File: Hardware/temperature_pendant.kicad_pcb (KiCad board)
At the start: 2 copper layers, 25.4 x 20.3 mm, 5 parts, among them J1 CONN-6, SW1 SW-MOM, U1 BLINKM/MINM, U2 TMP3X

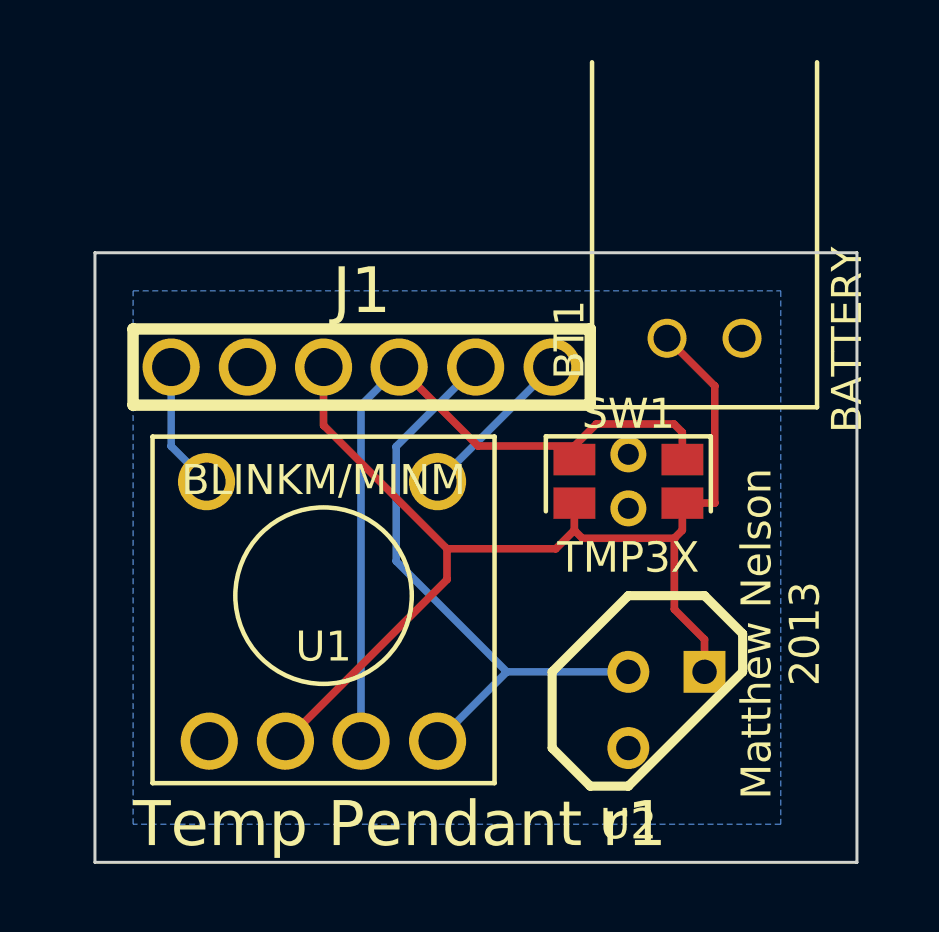
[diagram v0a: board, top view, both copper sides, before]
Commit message: Updated
Fixed same issues as in the bigger BlinkM version.  Re-did placement on
switch and battery connector.  Re-routed.
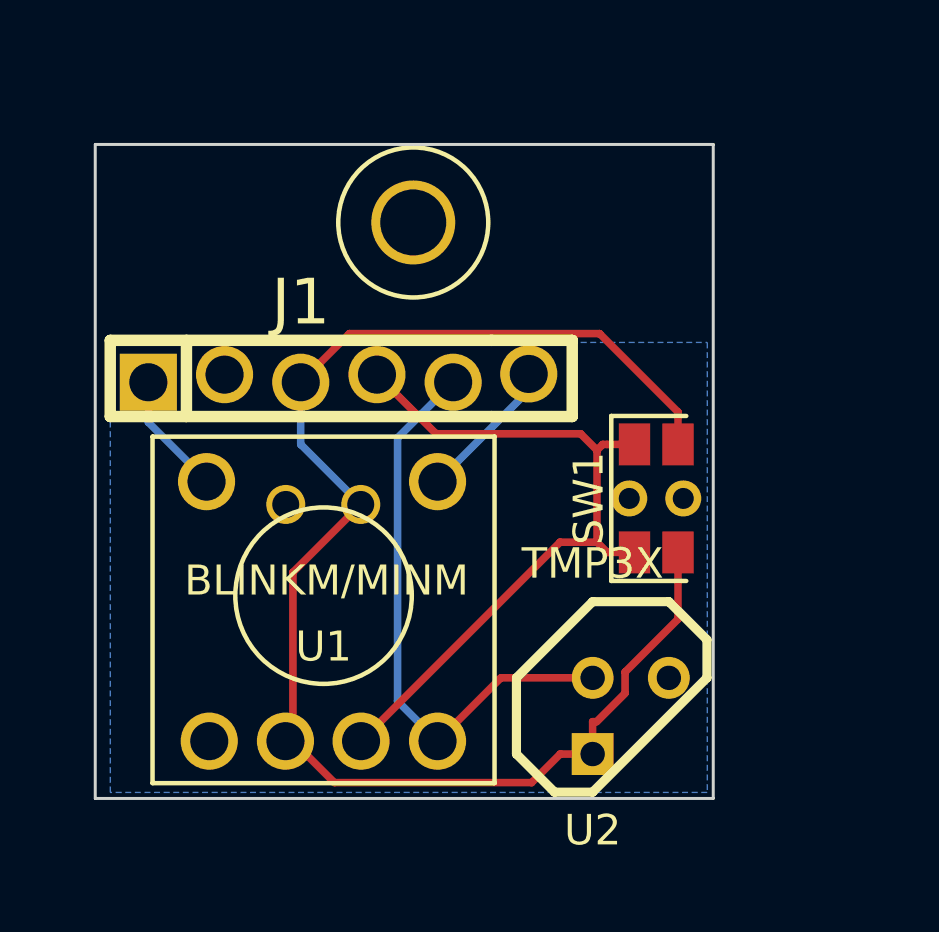
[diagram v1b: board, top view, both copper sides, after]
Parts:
- added MECH-HOLE220: VAL**, MECH-HOLE220, F.Cu at (210.0, 129.8)
- BT1: moved to B.Cu
- J1: footprint HDRV6W38P254_6X1 -> HDRV6W38P254_6X1-LOCK
- U2: footprint TO92 -> TO92-INVERT
- moved BT1 13.9 mm to (207.0, 130.0), turned to 180 degrees
- moved J1 2.07 mm to (206.2, 135.0)
- moved U2 1.21 mm to (217.2, 146.2)
- moved SW1 1.09 mm to (218.1, 139.0), turned to 90 degrees
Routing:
- net +BATT: track 38.6 -> 48.3 mm
- net TEMP: track 20.1 -> 19.3 mm
- net MISO: track 5.40 -> 4.85 mm
- net SW: track 25.3 -> 24.8 mm
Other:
- board size 25.4 x 20.3 mm -> 20.6 x 21.8 mm
- board text added: "Temp Pendant r2"
- board text removed: "Temp Pendant r1"
